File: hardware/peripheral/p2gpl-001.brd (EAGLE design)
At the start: 22 x 31 mm, 4 parts, among them J11 AUDIO_JACK_3.5MM_KIT

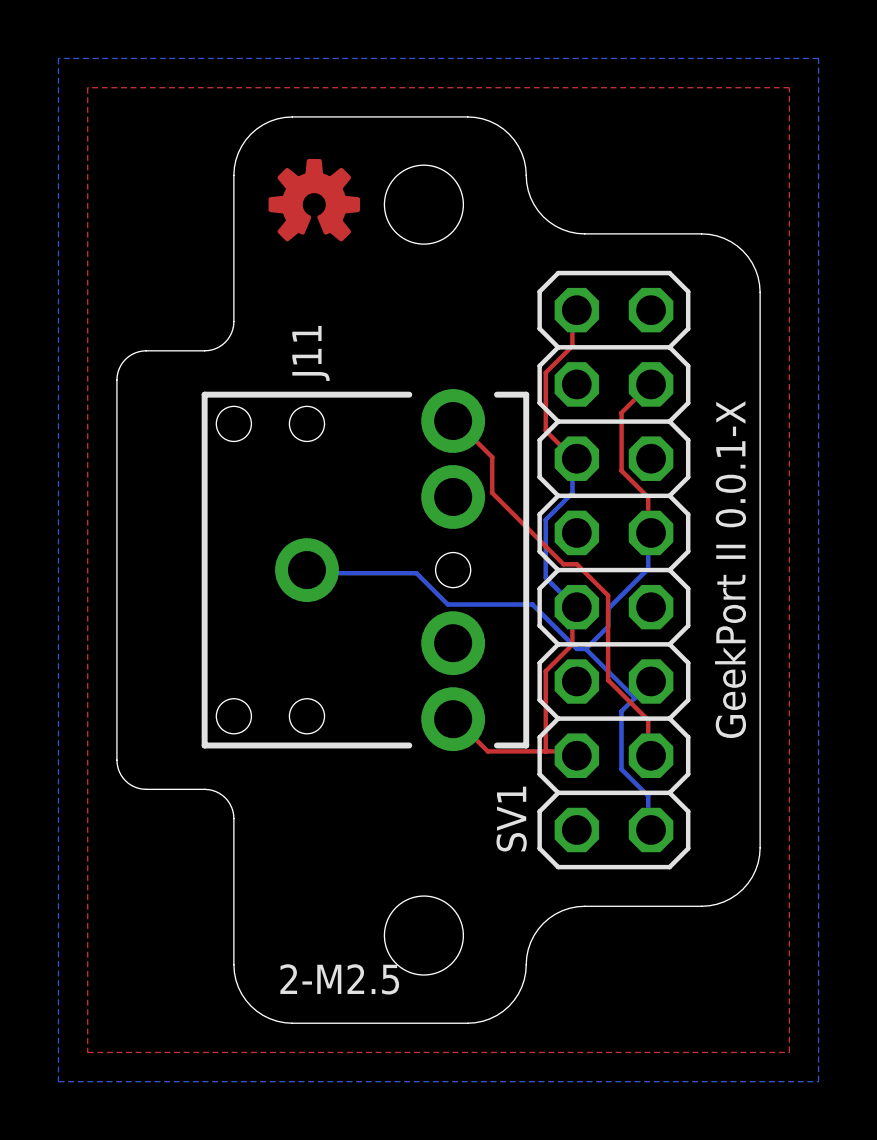
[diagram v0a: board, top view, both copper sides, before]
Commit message: Fixed polarity of 3.5mm jack.
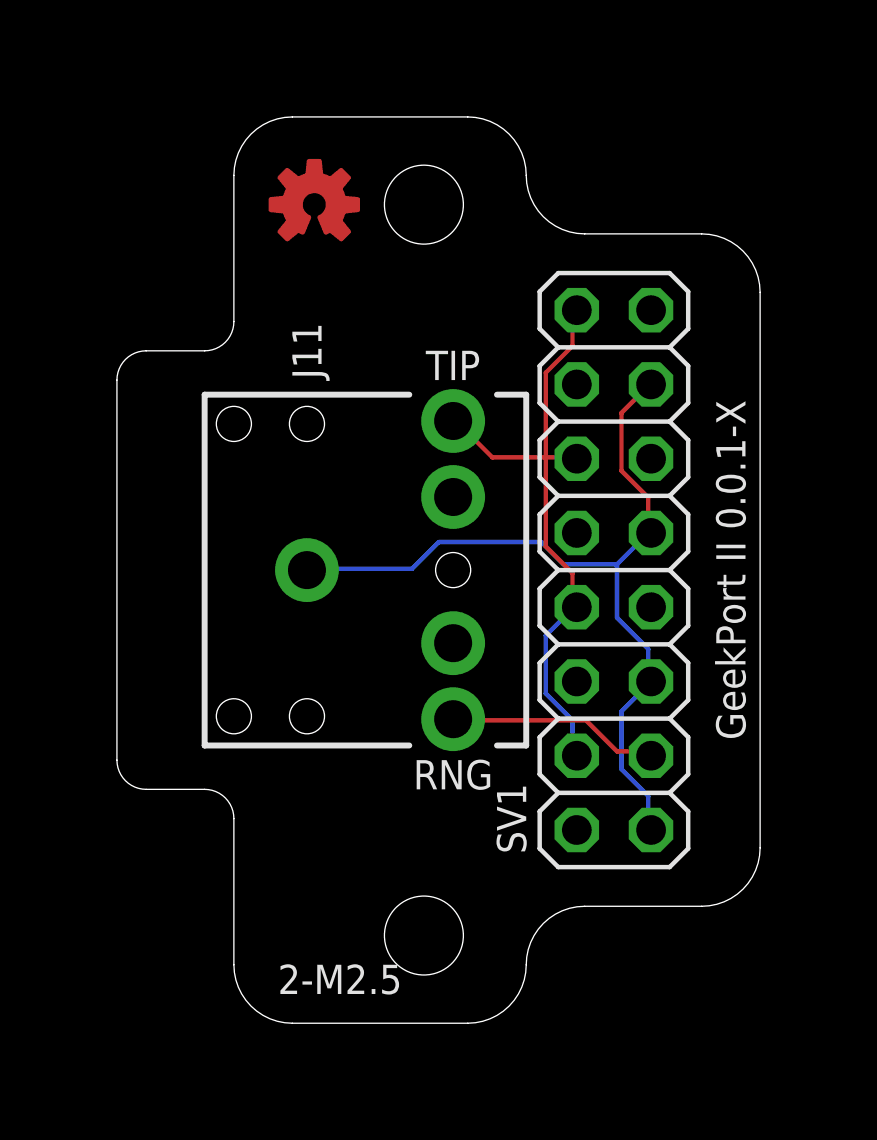
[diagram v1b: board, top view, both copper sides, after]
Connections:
- net ANLG0: now also J11.TIP; no longer J11.RING
- net VCC: now also J11.RING; no longer J11.TIP
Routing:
- net ANLG0: track 14.6 -> 7.30 mm
- net GND: track 29.8 -> 29.3 mm
- removed copper zone on layer 1, net GND
- removed copper zone on layer 16, net GND
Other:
- board text added: "RNG"
- board text added: "TIP"
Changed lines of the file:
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@@
 <rectangle x1="-4" y1="22" x2="1" y2="23" layer="42"/>
 <rectangle x1="-4" y1="8" x2="1" y2="9" layer="42"/>
+<text x="7.5" y="22.5" size="1" layer="25" align="center">TIP</text>
+<text x="7.5" y="8.5" size="1" layer="25" align="center">RNG</text>
 </plain>
 <attributes>
@@
 <contactref element="SV1" pad="13"/>
 <contactref element="J11" pad="SLEEVE"/>
+<wire x1="14.1732" y1="7.7724" x2="14.1732" y2="6.7056" width="0.1524" layer="16"/>
+<wire x1="13.2588" y1="8.6868" x2="14.1732" y2="7.7724" width="0.1524" layer="16"/>
+<wire x1="13.2588" y1="10.668" x2="13.2588" y2="8.6868" width="0.1524" layer="16"/>
+<wire x1="14.1732" y1="11.5824" x2="13.2588" y2="10.668" width="0.1524" layer="16"/>
+<wire x1="14.1732" y1="6.7056" x2="14.27" y2="6.61" width="0.1524" layer="16"/>
+<wire x1="14.1732" y1="11.5824" x2="14.27" y2="11.69" width="0.1524" layer="16"/>
 <wire x1="14.1732" y1="17.9832" x2="14.1732" y2="16.9164" width="0.1524" layer="1"/>
 <wire x1="13.2588" y1="18.8976" x2="14.1732" y2="17.9832" width="0.1524" layer="1"/>
@@
 <wire x1="14.1732" y1="16.9164" x2="14.27" y2="16.77" width="0.1524" layer="1"/>
 <wire x1="14.1732" y1="21.7932" x2="14.27" y2="21.85" width="0.1524" layer="1"/>
-<wire x1="14.1732" y1="7.7724" x2="14.1732" y2="6.7056" width="0.1524" layer="16"/>
-<wire x1="13.2588" y1="8.6868" x2="14.1732" y2="7.7724" width="0.1524" layer="16"/>
-<wire x1="13.2588" y1="10.668" x2="13.2588" y2="8.6868" width="0.1524" layer="16"/>
-<wire x1="14.1732" y1="11.5824" x2="13.716" y2="11.1252" width="0.1524" layer="16"/>
-<wire x1="13.716" y1="11.1252" x2="13.2588" y2="10.668" width="0.1524" layer="16"/>
-<wire x1="14.1732" y1="6.7056" x2="14.27" y2="6.61" width="0.1524" layer="16"/>
-<wire x1="14.1732" y1="11.5824" x2="14.27" y2="11.69" width="0.1524" layer="16"/>
-<wire x1="6.2484" y1="15.3924" x2="2.5908" y2="15.3924" width="0.1524" layer="16"/>
-<wire x1="7.3152" y1="14.3256" x2="6.2484" y2="15.3924" width="0.1524" layer="16"/>
-<wire x1="10.2108" y1="14.3256" x2="7.3152" y2="14.3256" width="0.1524" layer="16"/>
-<wire x1="11.7348" y1="12.8016" x2="10.2108" y2="14.3256" width="0.1524" layer="16"/>
-<wire x1="12.0396" y1="12.8016" x2="11.7348" y2="12.8016" width="0.1524" layer="16"/>
-<wire x1="13.716" y1="11.1252" x2="12.0396" y2="12.8016" width="0.1524" layer="16"/>
-<wire x1="2.5908" y1="15.3924" x2="2.5" y2="15.5" width="0.1524" layer="16"/>
-<wire x1="14.1732" y1="15.5448" x2="14.1732" y2="16.764" width="0.1524" layer="16"/>
-<wire x1="12.8016" y1="14.1732" x2="14.1732" y2="15.5448" width="0.1524" layer="16"/>
-<wire x1="12.8016" y1="13.5636" x2="12.8016" y2="14.1732" width="0.1524" layer="16"/>
-<wire x1="12.0396" y1="12.8016" x2="12.8016" y2="13.5636" width="0.1524" layer="16"/>
+<wire x1="6.096" y1="15.5448" x2="2.5908" y2="15.5448" width="0.1524" layer="16"/>
+<wire x1="7.0104" y1="16.4592" x2="6.096" y2="15.5448" width="0.1524" layer="16"/>
+<wire x1="10.5156" y1="16.4592" x2="7.0104" y2="16.4592" width="0.1524" layer="16"/>
+<wire x1="11.2776" y1="15.6972" x2="10.5156" y2="16.4592" width="0.1524" layer="16"/>
+<wire x1="13.1064" y1="15.6972" x2="11.2776" y2="15.6972" width="0.1524" layer="16"/>
+<wire x1="14.1732" y1="16.764" x2="13.1064" y2="15.6972" width="0.1524" layer="16"/>
+<wire x1="2.5908" y1="15.5448" x2="2.5" y2="15.5" width="0.1524" layer="16"/>
 <wire x1="14.1732" y1="16.764" x2="14.27" y2="16.77" width="0.1524" layer="16"/>
-<polygon width="0.2" layer="1">
-<vertex x="-5" y="-1"/>
-<vertex x="19" y="-1"/>
-<vertex x="19" y="32"/>
-<vertex x="-5" y="32"/>
-</polygon>
-<polygon width="0.2" layer="16">
-<vertex x="-6" y="-2"/>
-<vertex x="20" y="-2"/>
-<vertex x="20" y="33"/>
-<vertex x="-6" y="33"/>
-</polygon>
+<wire x1="14.1732" y1="12.8016" x2="14.1732" y2="11.7348" width="0.1524" layer="16"/>
+<wire x1="13.1064" y1="13.8684" x2="14.1732" y2="12.8016" width="0.1524" layer="16"/>
+<wire x1="13.1064" y1="15.6972" x2="13.1064" y2="13.8684" width="0.1524" layer="16"/>
+<wire x1="14.1732" y1="11.7348" x2="14.27" y2="11.69" width="0.1524" layer="16"/>
 </signal>
 <signal name="DTCT0">
@@
 <contactref element="SV1" pad="12"/>
 <contactref element="SV1" pad="8"/>
-<contactref element="J11" pad="TIP"/>
-<wire x1="8.6868" y1="9.2964" x2="10.668" y2="9.2964" width="0.1524" layer="1"/>
-<wire x1="10.668" y1="9.2964" x2="11.5824" y2="9.2964" width="0.1524" layer="1"/>
-<wire x1="7.62" y1="10.3632" x2="8.6868" y2="9.2964" width="0.1524" layer="1"/>
-<wire x1="11.5824" y1="9.2964" x2="11.73" y2="9.15" width="0.1524" layer="1"/>
-<wire x1="7.62" y1="10.3632" x2="7.5" y2="10.4" width="0.1524" layer="1"/>
-<wire x1="11.5824" y1="12.954" x2="11.5824" y2="14.1732" width="0.1524" layer="1"/>
-<wire x1="10.668" y1="12.0396" x2="11.5824" y2="12.954" width="0.1524" layer="1"/>
-<wire x1="10.668" y1="9.2964" x2="10.668" y2="12.0396" width="0.1524" layer="1"/>
-<wire x1="11.5824" y1="14.1732" x2="11.73" y2="14.23" width="0.1524" layer="1"/>
-<wire x1="11.5824" y1="18.1356" x2="11.5824" y2="19.2024" width="0.1524" layer="16"/>
-<wire x1="10.668" y1="17.2212" x2="11.5824" y2="18.1356" width="0.1524" layer="16"/>
-<wire x1="10.668" y1="15.24" x2="10.668" y2="17.2212" width="0.1524" layer="16"/>
-<wire x1="11.5824" y1="14.3256" x2="10.668" y2="15.24" width="0.1524" layer="16"/>
-<wire x1="11.5824" y1="19.2024" x2="11.73" y2="19.31" width="0.1524" layer="16"/>
-<wire x1="11.5824" y1="14.3256" x2="11.73" y2="14.23" width="0.1524" layer="16"/>
+<contactref element="J11" pad="RING"/>
+<wire x1="11.5824" y1="10.3632" x2="11.5824" y2="9.2964" width="0.1524" layer="16"/>
+<wire x1="10.668" y1="11.2776" x2="11.5824" y2="10.3632" width="0.1524" layer="16"/>
+<wire x1="10.668" y1="13.2588" x2="10.668" y2="11.2776" width="0.1524" layer="16"/>
+<wire x1="11.5824" y1="14.1732" x2="10.668" y2="13.2588" width="0.1524" layer="16"/>
+<wire x1="11.5824" y1="9.2964" x2="11.73" y2="9.15" width="0.1524" layer="16"/>
+<wire x1="11.5824" y1="14.1732" x2="11.73" y2="14.23" width="0.1524" layer="16"/>
+<wire x1="8.8392" y1="19.3548" x2="10.668" y2="19.3548" width="0.1524" layer="1"/>
+<wire x1="10.668" y1="19.3548" x2="11.5824" y2="19.3548" width="0.1524" layer="1"/>
+<wire x1="7.62" y1="20.574" x2="8.8392" y2="19.3548" width="0.1524" layer="1"/>
+<wire x1="11.5824" y1="19.3548" x2="11.73" y2="19.31" width="0.1524" layer="1"/>
+<wire x1="7.62" y1="20.574" x2="7.5" y2="20.6" width="0.1524" layer="1"/>
 <wire x1="11.5824" y1="23.1648" x2="11.5824" y2="24.384" width="0.1524" layer="1"/>
 <wire x1="10.668" y1="22.2504" x2="11.5824" y2="23.1648" width="0.1524" layer="1"/>
-<wire x1="10.668" y1="20.2692" x2="10.668" y2="22.2504" width="0.1524" layer="1"/>
-<wire x1="11.5824" y1="19.3548" x2="10.668" y2="20.2692" width="0.1524" layer="1"/>
+<wire x1="10.668" y1="19.3548" x2="10.668" y2="22.2504" width="0.1524" layer="1"/>
 <wire x1="11.5824" y1="24.384" x2="11.73" y2="24.39" width="0.1524" layer="1"/>
-<wire x1="11.5824" y1="19.3548" x2="11.73" y2="19.31" width="0.1524" layer="1"/>
+<wire x1="11.5824" y1="15.3924" x2="11.5824" y2="14.3256" width="0.1524" layer="1"/>
+<wire x1="10.668" y1="16.3068" x2="11.5824" y2="15.3924" width="0.1524" layer="1"/>
+<wire x1="10.668" y1="19.3548" x2="10.668" y2="16.3068" width="0.1524" layer="1"/>
+<wire x1="11.5824" y1="14.3256" x2="11.73" y2="14.23" width="0.1524" layer="1"/>
 </signal>
 <signal name="DTCT1">
@@
 <signal name="ANLG0">
 <contactref element="SV1" pad="3"/>
-<contactref element="J11" pad="RING"/>
-<wire x1="14.1732" y1="10.3632" x2="14.1732" y2="9.2964" width="0.1524" layer="1"/>
-<wire x1="12.8016" y1="11.7348" x2="14.1732" y2="10.3632" width="0.1524" layer="1"/>
-<wire x1="12.8016" y1="14.6304" x2="12.8016" y2="11.7348" width="0.1524" layer="1"/>
-<wire x1="11.7348" y1="15.6972" x2="12.8016" y2="14.6304" width="0.1524" layer="1"/>
-<wire x1="11.2776" y1="15.6972" x2="11.7348" y2="15.6972" width="0.1524" layer="1"/>
-<wire x1="8.8392" y1="18.1356" x2="11.2776" y2="15.6972" width="0.1524" layer="1"/>
-<wire x1="8.8392" y1="19.3548" x2="8.8392" y2="18.1356" width="0.1524" layer="1"/>
-<wire x1="7.62" y1="20.574" x2="8.8392" y2="19.3548" width="0.1524" layer="1"/>
+<contactref element="J11" pad="TIP"/>
+<wire x1="13.1064" y1="9.2964" x2="14.1732" y2="9.2964" width="0.1524" layer="1"/>
+<wire x1="12.0396" y1="10.3632" x2="13.1064" y2="9.2964" width="0.1524" layer="1"/>
+<wire x1="7.62" y1="10.3632" x2="12.0396" y2="10.3632" width="0.1524" layer="1"/>
 <wire x1="14.1732" y1="9.2964" x2="14.27" y2="9.15" width="0.1524" layer="1"/>
-<wire x1="7.62" y1="20.574" x2="7.5" y2="20.6" width="0.1524" layer="1"/>
+<wire x1="7.62" y1="10.3632" x2="7.5" y2="10.4" width="0.1524" layer="1"/>
 </signal>
 <signal name="ANLG1">
